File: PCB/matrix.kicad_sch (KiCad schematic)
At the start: 103 parts

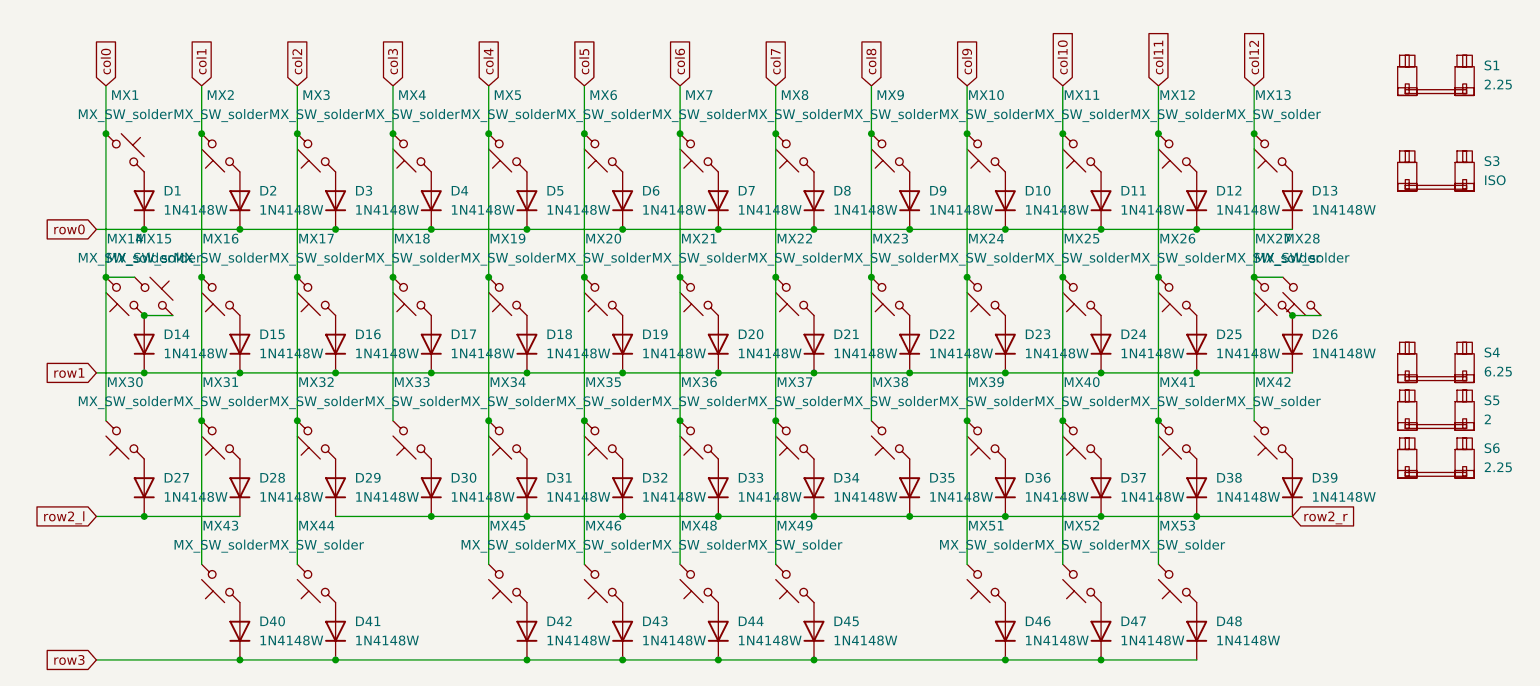
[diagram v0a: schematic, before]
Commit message: More files added
Gerber files for PCB along with BOM and CPL files. Also added picture of supported layouts
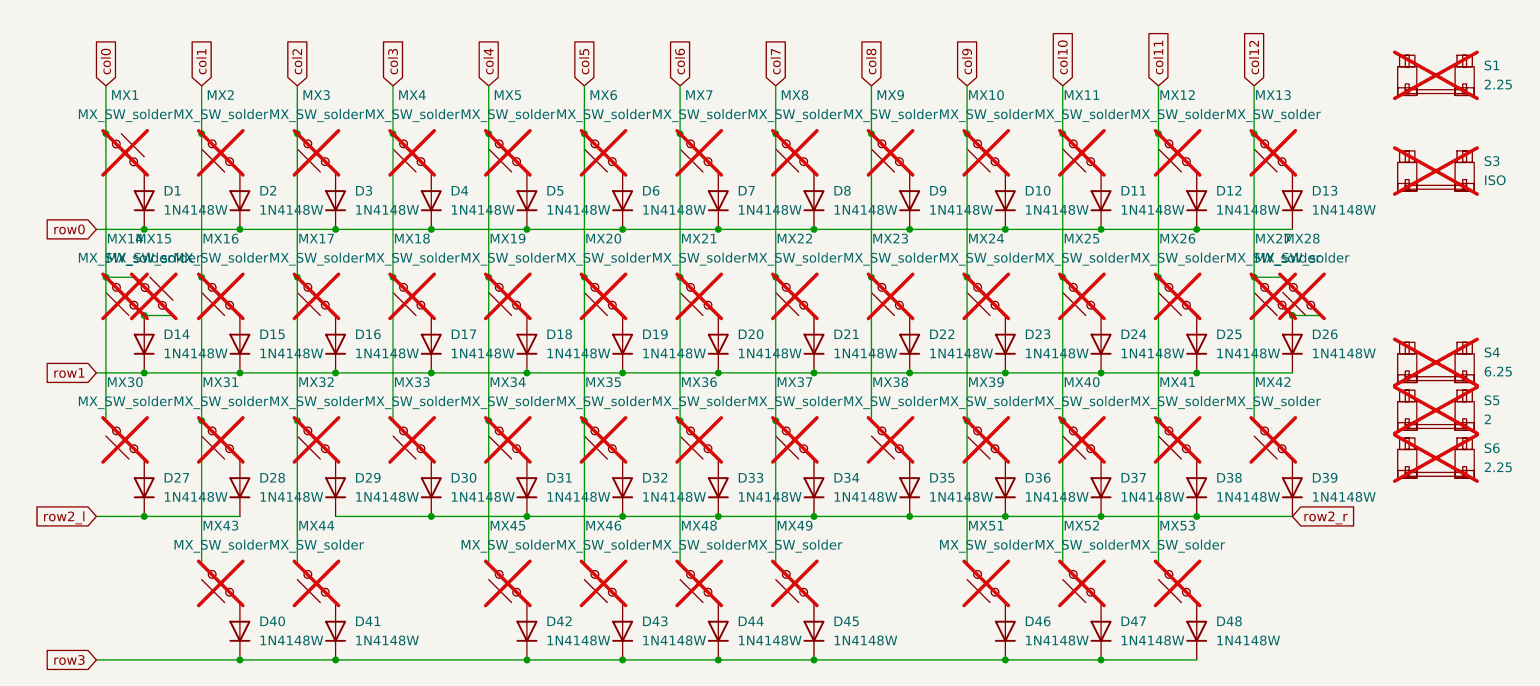
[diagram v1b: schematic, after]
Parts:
- MX1, MX10, MX11, MX12, MX13, MX14, MX15, MX16, MX17, MX18, MX19, MX2, MX20, MX21, MX22, MX23, MX24, MX25, MX26, MX27, MX28, MX3, MX30, MX31, MX32, MX33, MX34, MX35, MX36, MX37, MX38, MX39, MX4, MX40, MX41, MX42, MX43, MX44, MX45, MX46, MX48, MX49, MX5, MX51, MX52, MX53, MX6, MX7, MX8, MX9, S1, S3, S4, S5, S6: now not fitted
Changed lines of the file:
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@@
 		(in_bom yes)
 		(on_board yes)
-		(dnp no)
+		(dnp yes)
 		(fields_autoplaced yes)
 		(property "Reference" "MX2"
@@
 		(in_bom yes)
 		(on_board yes)
-		(dnp no)
+		(dnp yes)
 		(fields_autoplaced yes)
 		(property "Reference" "MX21"
@@
 		(in_bom yes)
 		(on_board yes)
-		(dnp no)
+		(dnp yes)
 		(fields_autoplaced yes)
 		(property "Reference" "MX40"
@@
 		(in_bom yes)
 		(on_board yes)
-		(dnp no)
+		(dnp yes)
 		(fields_autoplaced yes)
 		(property "Reference" "MX25"
@@
 		(in_bom yes)
 		(on_board yes)
-		(dnp no)
+		(dnp yes)
 		(fields_autoplaced yes)
 		(property "Reference" "MX28"
@@
 		(in_bom yes)
 		(on_board yes)
-		(dnp no)
+		(dnp yes)
 		(fields_autoplaced yes)
 		(property "Reference" "MX33"
@@
 		(in_bom yes)
 		(on_board yes)
-		(dnp no)
+		(dnp yes)
 		(fields_autoplaced yes)
 		(property "Reference" "S5"
@@
 		(in_bom yes)
 		(on_board yes)
-		(dnp no)
+		(dnp yes)
 		(fields_autoplaced yes)
 		(property "Reference" "MX23"
@@
 		(in_bom yes)
 		(on_board yes)
-		(dnp no)
+		(dnp yes)
 		(fields_autoplaced yes)
 		(property "Reference" "MX41"
@@
 		(in_bom yes)
 		(on_board yes)
-		(dnp no)
+		(dnp yes)
 		(fields_autoplaced yes)
 		(property "Reference" "MX22"
@@
 		(in_bom yes)
 		(on_board yes)
-		(dnp no)
+		(dnp yes)
 		(fields_autoplaced yes)
 		(property "Reference" "MX32"
@@
 		(in_bom yes)
 		(on_board yes)
-		(dnp no)
+		(dnp yes)
 		(fields_autoplaced yes)
 		(property "Reference" "MX6"
@@
 		(in_bom yes)
 		(on_board yes)
-		(dnp no)
+		(dnp yes)
 		(fields_autoplaced yes)
 		(property "Reference" "MX48"
@@
 		(in_bom yes)
 		(on_board yes)
-		(dnp no)
+		(dnp yes)
 		(fields_autoplaced yes)
 		(property "Reference" "MX1"
@@
 		(in_bom yes)
 		(on_board yes)
-		(dnp no)
+		(dnp yes)
 		(fields_autoplaced yes)
 		(property "Reference" "MX10"
@@
 		(in_bom yes)
 		(on_board yes)
-		(dnp no)
+		(dnp yes)
 		(fields_autoplaced yes)
 		(property "Reference" "MX15"
@@
 		(in_bom yes)
 		(on_board yes)
-		(dnp no)
+		(dnp yes)
 		(property "Reference" "MX14"
 			(at 25.4 41.91 0)
@@
 		(in_bom yes)
 		(on_board yes)
-		(dnp no)
+		(dnp yes)
 		(fields_autoplaced yes)
 		(property "Reference" "MX43"
@@
 		(in_bom yes)
 		(on_board yes)
-		(dnp no)
+		(dnp yes)
 		(fields_autoplaced yes)
 		(property "Reference" "MX53"
@@
 		(in_bom yes)
 		(on_board yes)
-		(dnp no)
+		(dnp yes)
 		(fields_autoplaced yes)
 		(property "Reference" "MX11"
@@
 		(in_bom yes)
 		(on_board yes)
-		(dnp no)
+		(dnp yes)
 		(fields_autoplaced yes)
 		(property "Reference" "MX36"
@@
 		(in_bom yes)
 		(on_board yes)
-		(dnp no)
+		(dnp yes)
 		(fields_autoplaced yes)
 		(property "Reference" "MX4"
@@
 		(in_bom yes)
 		(on_board yes)
-		(dnp no)
+		(dnp yes)
 		(fields_autoplaced yes)
 		(property "Reference" "S4"
@@
 		(in_bom yes)
 		(on_board yes)
-		(dnp no)
+		(dnp yes)
 		(fields_autoplaced yes)
 		(property "Reference" "MX26"
@@
 		(in_bom yes)
 		(on_board yes)
-		(dnp no)
+		(dnp yes)
 		(fields_autoplaced yes)
 		(property "Reference" "MX52"
@@
 		(in_bom yes)
 		(on_board yes)
-		(dnp no)
+		(dnp yes)
 		(fields_autoplaced yes)
 		(property "Reference" "MX3"
@@
 		(in_bom yes)
 		(on_board yes)
-		(dnp no)
+		(dnp yes)
 		(fields_autoplaced yes)
 		(property "Reference" "S1"
@@
 		(in_bom yes)
 		(on_board yes)
-		(dnp no)
+		(dnp yes)
 		(fields_autoplaced yes)
 		(property "Reference" "MX16"
@@
 		(in_bom yes)
 		(on_board yes)
-		(dnp no)
+		(dnp yes)
 		(fields_autoplaced yes)
 		(property "Reference" "MX18"
@@
 		(in_bom yes)
 		(on_board yes)
-		(dnp no)
+		(dnp yes)
 		(fields_autoplaced yes)
 		(property "Reference" "S3"
@@
 		(in_bom yes)
 		(on_board yes)
-		(dnp no)
+		(dnp yes)
 		(fields_autoplaced yes)
 		(property "Reference" "MX31"
@@
 		(in_bom yes)
 		(on_board yes)
-		(dnp no)
+		(dnp yes)
 		(fields_autoplaced yes)
 		(property "Reference" "MX45"
@@
 		(in_bom yes)
 		(on_board yes)
-		(dnp no)
+		(dnp yes)
 		(fields_autoplaced yes)
 		(property "Reference" "MX37"
@@
 		(in_bom yes)
 		(on_board yes)
-		(dnp no)
+		(dnp yes)
 		(fields_autoplaced yes)
 		(property "Reference" "MX30"
@@
 		(in_bom yes)
 		(on_board yes)
-		(dnp no)
+		(dnp yes)
 		(fields_autoplaced yes)
 		(property "Reference" "MX20"
@@
 		(in_bom yes)
 		(on_board yes)
-		(dnp no)
+		(dnp yes)
 		(fields_autoplaced yes)
 		(property "Reference" "MX12"
@@
 		(in_bom yes)
 		(on_board yes)
-		(dnp no)
+		(dnp yes)
 		(fields_autoplaced yes)
 		(property "Reference" "MX44"
@@
 		(in_bom yes)
 		(on_board yes)
-		(dnp no)
+		(dnp yes)
 		(fields_autoplaced yes)
 		(property "Reference" "MX9"
@@
 		(in_bom yes)
 		(on_board yes)
-		(dnp no)
+		(dnp yes)
 		(fields_autoplaced yes)
 		(property "Reference" "MX39"
@@
 		(in_bom yes)
 		(on_board yes)
-		(dnp no)
+		(dnp yes)
 		(fields_autoplaced yes)
 		(property "Reference" "MX51"
@@
 		(in_bom yes)
 		(on_board yes)
-		(dnp no)
+		(dnp yes)
 		(fields_autoplaced yes)
 		(property "Reference" "MX7"
@@
 		(in_bom yes)
 		(on_board yes)
-		(dnp no)
+		(dnp yes)
 		(fields_autoplaced yes)
 		(property "Reference" "MX24"
@@
 		(in_bom yes)
 		(on_board yes)
-		(dnp no)
+		(dnp yes)
 		(fields_autoplaced yes)
 		(property "Reference" "MX34"
@@
 		(in_bom yes)
 		(on_board yes)
-		(dnp no)
+		(dnp yes)
 		(fields_autoplaced yes)
 		(property "Reference" "MX46"
@@
 		(in_bom yes)
 		(on_board yes)
-		(dnp no)
+		(dnp yes)
 		(fields_autoplaced yes)
 		(property "Reference" "MX49"
@@
 		(in_bom yes)
 		(on_board yes)
-		(dnp no)
+		(dnp yes)
 		(fields_autoplaced yes)
 		(property "Reference" "MX42"
@@
 		(in_bom yes)
 		(on_board yes)
-		(dnp no)
+		(dnp yes)
 		(fields_autoplaced yes)
 		(property "Reference" "MX19"
@@
 		(in_bom yes)
 		(on_board yes)
-		(dnp no)
+		(dnp yes)
 		(fields_autoplaced yes)
 		(property "Reference" "MX5"
@@
 		(in_bom yes)
 		(on_board yes)
-		(dnp no)
+		(dnp yes)
 		(fields_autoplaced yes)
 		(property "Reference" "MX17"
@@
 		(in_bom yes)
 		(on_board yes)
-		(dnp no)
+		(dnp yes)
 		(fields_autoplaced yes)
 		(property "Reference" "MX35"
@@
 		(in_bom yes)
 		(on_board yes)
-		(dnp no)
+		(dnp yes)
 		(fields_autoplaced yes)
 		(property "Reference" "MX8"
@@
 		(in_bom yes)
 		(on_board yes)
-		(dnp no)
+		(dnp yes)
 		(fields_autoplaced yes)
 		(property "Reference" "MX27"
@@
 		(in_bom yes)
 		(on_board yes)
-		(dnp no)
+		(dnp yes)
 		(fields_autoplaced yes)
 		(property "Reference" "MX38"
@@
 		(in_bom yes)
 		(on_board yes)
-		(dnp no)
+		(dnp yes)
 		(fields_autoplaced yes)
 		(property "Reference" "MX13"
@@
 		(in_bom yes)
 		(on_board yes)
-		(dnp no)
+		(dnp yes)
 		(fields_autoplaced yes)
 		(property "Reference" "S6"

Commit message: PCB Fab v1
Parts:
- removed D25, D28, D42, D43, D45, D46: 1N4148W, Diode_SMD:D_SOD-123, symbol Diode:1N4148W
- removed MX26, MX28, MX31, MX45, MX46, MX49, MX51: MX_SW_solder, PCM_marbastlib-mx:SW_MX_1u, symbol PCM_marbastlib-mx:MX_SW_HS
- removed S1, S6: 2.25, PCM_marbastlib-mx:STAB_MX_P_2.25u, symbol PCM_marbastlib-mx:MX_stab
- removed S3: ISO, PCM_marbastlib-mx:STAB_MX_P_ISO-ROT, symbol PCM_marbastlib-mx:MX_stab
- removed S5: 2, PCM_marbastlib-mx:STAB_MX_P_2u, symbol PCM_marbastlib-mx:MX_stab
- added S2: 2.25, PCM_marbastlib-mx:STAB_MX_P_2.25u, symbol PCM_marbastlib-mx:MX_stab
- D1, D10, D11, D12, D13, D14, D15, D16, D17, D18, D19, D2, D20, D21, D22, D23, D24, D26, D27, D29, D3, D30, D31, D32, D33, D34, D35, D36, D37, D38, D39, D4, D40, D41, D44, D47, D48, D5, D6, D7, D8, D9: LCSC C7420318 -> (none)
- MX1, MX10, MX11, MX12, MX14, MX15, MX16, MX17, MX18, MX19, MX2, MX20, MX21, MX22, MX23, MX24, MX25, MX3, MX32, MX33, MX34, MX35, MX36, MX37, MX38, MX39, MX4, MX40, MX43, MX44, MX48, MX5, MX52, MX53, MX6, MX7, MX8, MX9: now fitted
- MX13: footprint PCM_marbastlib-mx:SW_MX_1.5u -> PCM_marbastlib-mx:SW_MX_1u; now fitted
- MX27: footprint PCM_marbastlib-mx:SW_MX_1u -> PCM_marbastlib-mx:SW_MX_1.75u; now fitted
- MX30: footprint PCM_marbastlib-mx:SW_MX_1.25u -> PCM_marbastlib-mx:SW_MX_1u; now fitted
- MX41: footprint PCM_marbastlib-mx:SW_MX_1u -> PCM_marbastlib-mx:SW_MX_1.25u; now fitted
- MX42: footprint PCM_marbastlib-mx:SW_MX_1.75u -> PCM_marbastlib-mx:SW_MX_1u; now fitted
- S1: renamed from S4; now fitted

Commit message: updates
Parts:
- removed D12, D24, D37: 1N4148W, Diode_SMD:D_SOD-123, symbol Diode:1N4148W
- removed MX12, MX25, MX40: MX_SW_solder, PCM_marbastlib-mx:SW_MX_1u, symbol PCM_marbastlib-mx:MX_SW_HS
- added S3: 2.25, PCM_marbastlib-mx:STAB_MX_P_2.25u, symbol PCM_marbastlib-mx:MX_stab
- MX13: footprint PCM_marbastlib-mx:SW_MX_1u -> PCM_marbastlib-mx:SW_MX_1.5u
- MX27: footprint PCM_marbastlib-mx:SW_MX_1.75u -> PCM_marbastlib-mx:SW_MX_1u
- MX41: footprint PCM_marbastlib-mx:SW_MX_1.25u -> PCM_marbastlib-mx:SW_MX_1.75u
- MX44, MX52: footprint PCM_marbastlib-mx:SW_MX_1.5u -> PCM_marbastlib-mx:SW_MX_1.25u
- renumbered D13 to D12, D14 to D13, D15 to D14, D16 to D15, D17 to D16, D18 to D17, D19 to D18, D20 to D19, D21 to D20, D22 to D21, D23 to D22, D26 to D23, D27 to D24, D29 to D25, D30 to D26, D31 to D27, D32 to D28, D33 to D29, D34 to D30, D35 to D31, D36 to D32, D38 to D33, D39 to D34, D40 to D35, D41 to D36, D44 to D37, D47 to D38, D48 to D39
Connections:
- net col12 is gone; now on net col11: MX13.2, MX27.2, MX42.2
- net col10: now also MX41.1
- net col11: no longer MX41.2
- net col2: now also MX44.1; no longer MX44.2
- net at D33.2 (A): now also MX41.2; no longer MX41.1
- net at D36.2 (A): now also MX44.2; no longer MX44.1
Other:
- moved on the sheet: D12, D23, D33, D34, MX13, MX27, MX41, MX42, MX44

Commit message: back to the drawing board
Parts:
- added D40, D41, D42, D43: 1N4148W, Diode_SMD:D_SOD-123, symbol Diode:1N4148W
- added MX38, MX40, MX41, MX43, MX45, MX47: MX_SW_solder, PCM_marbastlib-mx:SW_MX_1u, symbol PCM_marbastlib-mx:MX_SW_solder
- added MX39, MX44: MX_SW_solder, PCM_marbastlib-mx:SW_MX_1.25u, symbol PCM_marbastlib-mx:MX_SW_solder
- added S4, S5: 2, PCM_marbastlib-mx:STAB_MX_P_2u, symbol PCM_marbastlib-mx:MX_stab
- MX36: renamed from MX43; footprint PCM_marbastlib-mx:SW_MX_1u -> PCM_marbastlib-mx:SW_MX_1.25u
- MX48: renamed from MX53; footprint PCM_marbastlib-mx:SW_MX_1u -> PCM_marbastlib-mx:SW_MX_1.25u
- S1: value 6.25 -> 7; footprint PCM_marbastlib-mx:STAB_MX_P_6.25u -> PCM_marbastlib-mx:STAB_MX_P_7u
- renumbered MX13 to MX12, MX14 to MX13, MX15 to MX14, MX16 to MX15, MX17 to MX16, MX18 to MX17, MX19 to MX18, MX20 to MX19, MX21 to MX20, MX22 to MX21, MX23 to MX22, MX24 to MX23, MX27 to MX24, MX30 to MX25, MX32 to MX26, MX33 to MX27, MX34 to MX28, MX35 to MX29, MX36 to MX30, MX37 to MX31, MX38 to MX32, MX39 to MX33, MX41 to MX34, MX42 to MX35, MX44 to MX37, MX48 to MX42, MX52 to MX46
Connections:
- net row2_r is gone; now on net row2: D25.1 (K), D26.1 (K), D27.1 (K), D28.1 (K), D29.1 (K), D30.1 (K), D31.1 (K), D32.1 (K), D33.1 (K), D34.1 (K)
- net col0: now also MX25.1, MX36.2; no longer MX25.2
- net col1: no longer MX36.2
- net col10: now also MX47.2
- net col2: now also MX37.2, MX38.2; no longer MX37.1
- net col3: now also MX39.2, MX40.2
- net col4: now also MX41.2
- net col7: now also MX43.2
- net col9: now also MX44.2, MX45.2
- net row3: now also D40.1 (K), D41.1 (K), D42.1 (K), D43.1 (K)
- net at D37.2 (A): now also MX39.1, MX40.1; no longer MX42.1
- net at D24.2 (A): now also MX25.2; no longer MX25.1
- net at D36.2 (A): now also MX37.1, MX38.1; no longer MX37.2
- net at D39.2 (A): now also MX42.1; no longer MX48.1
- net at D38.2 (A): now also MX41.1; no longer MX46.1
- net row2_l renamed row2
- new net: D41.2 (A), MX44.1, MX45.1
- new net: D40.2 (A), MX43.1
- new net: D43.2 (A), MX48.1
- new net: D42.2 (A), MX46.1, MX47.1
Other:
- moved on the sheet: D35, D37, D38, D39, MX25, MX36, MX37

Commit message: beeg overhaul and new layout image
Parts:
- removed MX36: MX_SW_solder, PCM_marbastlib-mx:SW_MX_1.25u, symbol PCM_marbastlib-mx:MX_SW_HS
- removed MX42: MX_SW_solder, PCM_marbastlib-mx:SW_MX_1u, symbol PCM_marbastlib-mx:MX_SW_HS
- added D25: 1N4148W, Diode_SMD:D_SOD-123, symbol Diode:1N4148W
- added MX26, MX38: MX_SW_solder, PCM_marbastlib-mx:SW_MX_1.25u, symbol PCM_marbastlib-mx:MX_SW_solder
- added MX27, MX44, MX45: MX_SW_solder, PCM_marbastlib-mx:SW_MX_1u, symbol PCM_marbastlib-mx:MX_SW_solder
- added S6: 6.25, PCM_marbastlib-mx:STAB_MX_P_6.25u, symbol PCM_marbastlib-mx:MX_stab
- renumbered D25 to D26, D26 to D27, D27 to D28, D28 to D29, D29 to D30, D30 to D31, D31 to D32, D32 to D33, D33 to D34, D34 to D35, D35 to D36, D36 to D37, D37 to D38, D38 to D39, D39 to D40, D40 to D41, D41 to D42, D42 to D43, D43 to D44, MX26 to MX28, MX27 to MX29, MX28 to MX30, MX29 to MX31, MX30 to MX32, MX31 to MX33, MX32 to MX34, MX33 to MX35, MX34 to MX36, MX35 to MX37, MX37 to MX39, MX38 to MX40, MX39 to MX41, MX40 to MX42, MX41 to MX43, MX43 to MX46, MX44 to MX47, MX45 to MX48, MX46 to MX49, MX47 to MX50, MX48 to MX51
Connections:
- net col0: now also MX25.2, MX26.2, MX38.2; no longer MX25.1
- net col1: now also MX27.2
- net col6: now also MX44.2, MX45.2
- net row2: now also D25.1 (K)
- net at D24.2 (A): now also MX25.1, MX26.1; no longer MX25.2
- net at D40.2 (A): now also MX44.1, MX45.1
- net at D36.2 (A): now also MX38.1
- new net: D25.2 (A), MX27.1
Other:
- moved on the sheet: MX25
